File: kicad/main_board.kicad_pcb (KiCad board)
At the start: 2 copper layers, 42 x 67 mm, 65 parts, among them J1 Conn_01x18, J2 Conn_01x18, J3 Conn_01x07, J4 Conn_01x07, J5 Conn_01x07, J6 Conn_01x07, J7 Conn_01x07, J8 TYPE-C-31-M-12, J9 TYPE-C-31-M-12, Q1 DMG2301L-7, Q2 DMG2301L-7, Q3 DMG2301L-7, Q4 DMG2301L-7, Q5 DMG2301L-7, SW1 Reset, SW2 Boot, U1 XC6220B331MR, U2 RP2040, U3 W25Q128JVS, U4 COS724, U5 COS724, U6 USBLC6-2SC6, U7 USBLC6-2SC6, Y1 Crystal_GND24

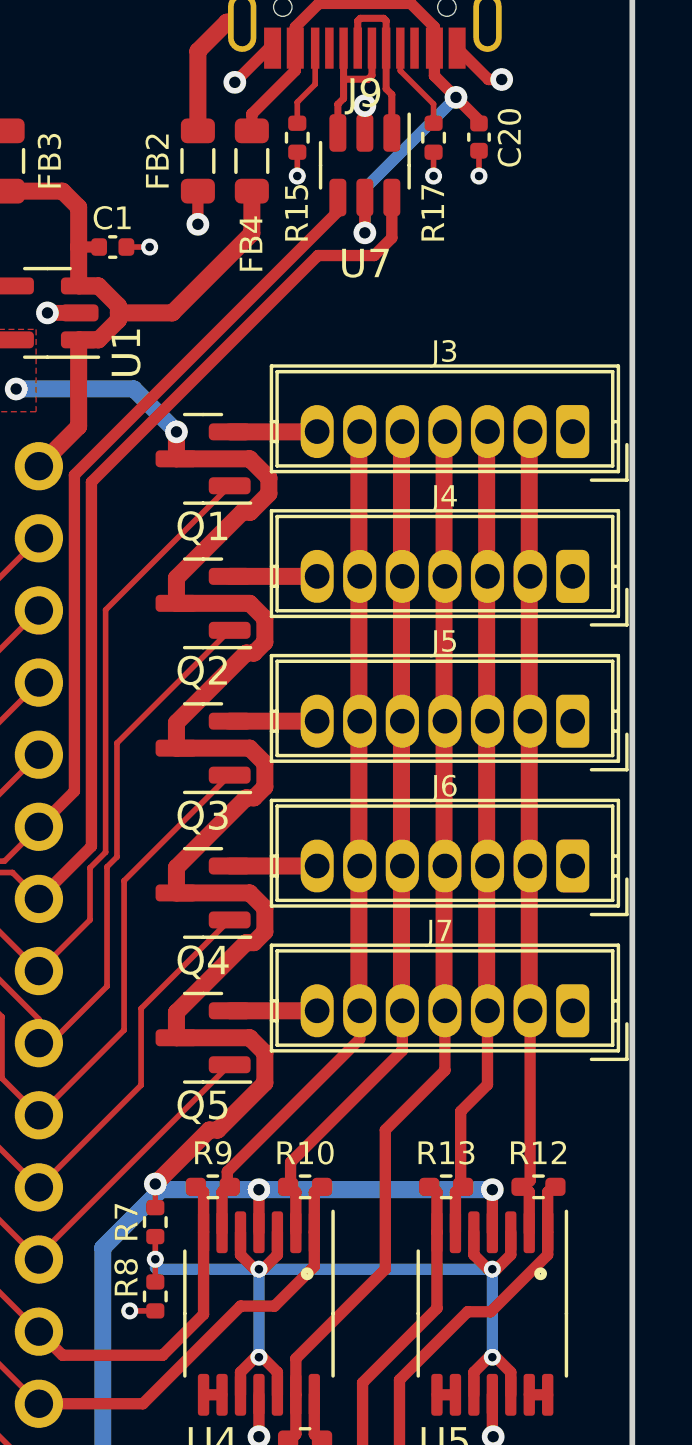
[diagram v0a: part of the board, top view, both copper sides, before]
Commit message: refactor pcb file and add kicad footprint file
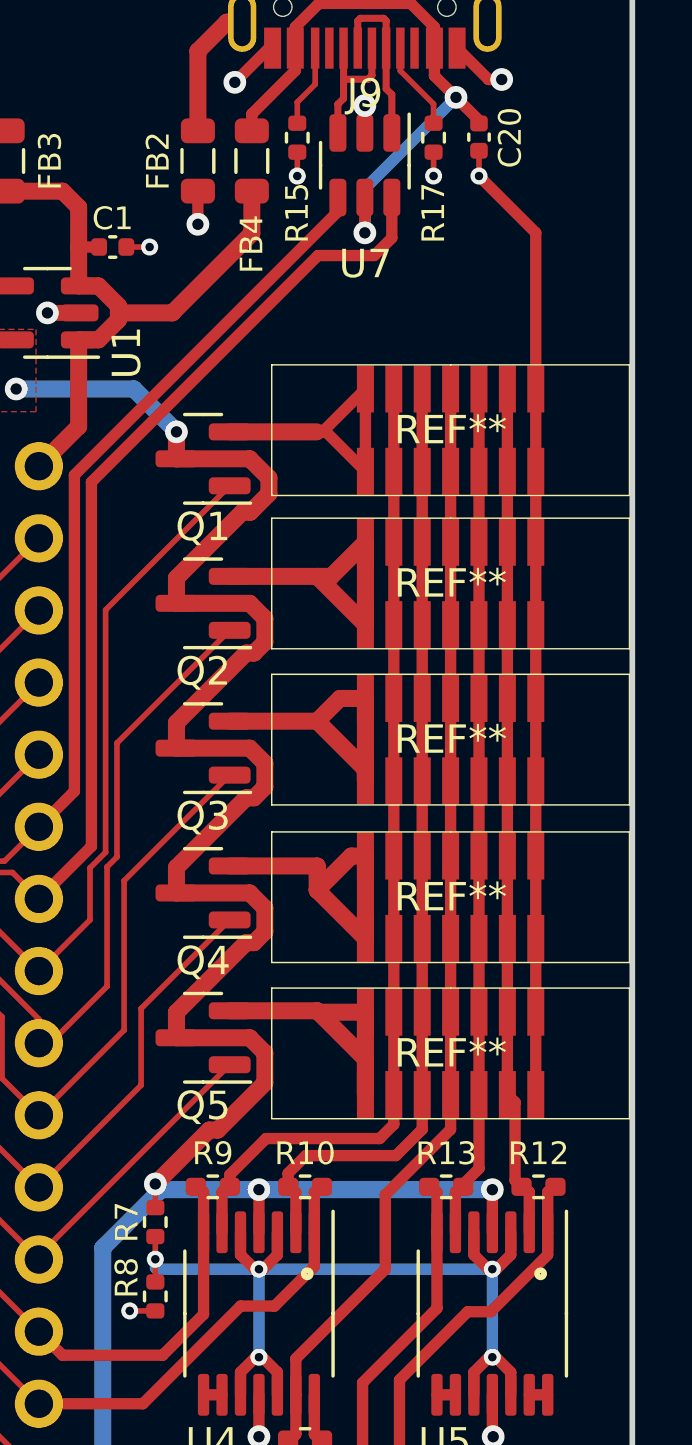
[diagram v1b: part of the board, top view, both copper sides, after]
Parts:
- removed J3, J4, J5, J6, J7: Conn_01x07, lalboard:JST_ZH_B7B-ZR_1x07_P1.50mm_Vertical
- added REF**: AMP Connectors TE Connectivity-1734248-7, user:AMP Connectors TE Connectivity-1734248-7, F.Cu at (185.6, 59.5)
- added REF**: AMP Connectors TE Connectivity-1734248-7, user:AMP Connectors TE Connectivity-1734248-7, F.Cu at (185.6, 54.0)
- added REF**: AMP Connectors TE Connectivity-1734248-7, user:AMP Connectors TE Connectivity-1734248-7, F.Cu at (185.6, 76.0)
- added REF**: AMP Connectors TE Connectivity-1734248-7, user:AMP Connectors TE Connectivity-1734248-7, F.Cu at (185.6, 70.5)
- added REF**: AMP Connectors TE Connectivity-1734248-7, user:AMP Connectors TE Connectivity-1734248-7, F.Cu at (185.6, 65.0)
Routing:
- net GND: track 49.5 -> 82.7 mm
- net Net-(J6-Pin_7): track 3.08 -> 11.4 mm
- net Net-(J7-Pin_7): track 3.08 -> 11.4 mm
- net Net-(J5-Pin_7): track 3.08 -> 10.8 mm
- net Net-(J3-Pin_7): track 3.08 -> 10.6 mm
- net Net-(J4-Pin_7): track 3.08 -> 10.6 mm
- net /COL2: track 29.3 -> 33.6 mm
- net /COL1: track 30.7 -> 34.5 mm
- net /COL5: track 27.5 -> 30.0 mm
- net /COL3: track 36.9 -> 39.3 mm
- net /COL4: track 27.8 -> 30.0 mm
